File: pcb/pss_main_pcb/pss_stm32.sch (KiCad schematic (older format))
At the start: 24 parts, among them J5 STM32_Prog, SW1 Hot Air Gun Input, SW2 Soldering Iron Input, SW3 SW_Push, U5 STM32F030K6Tx

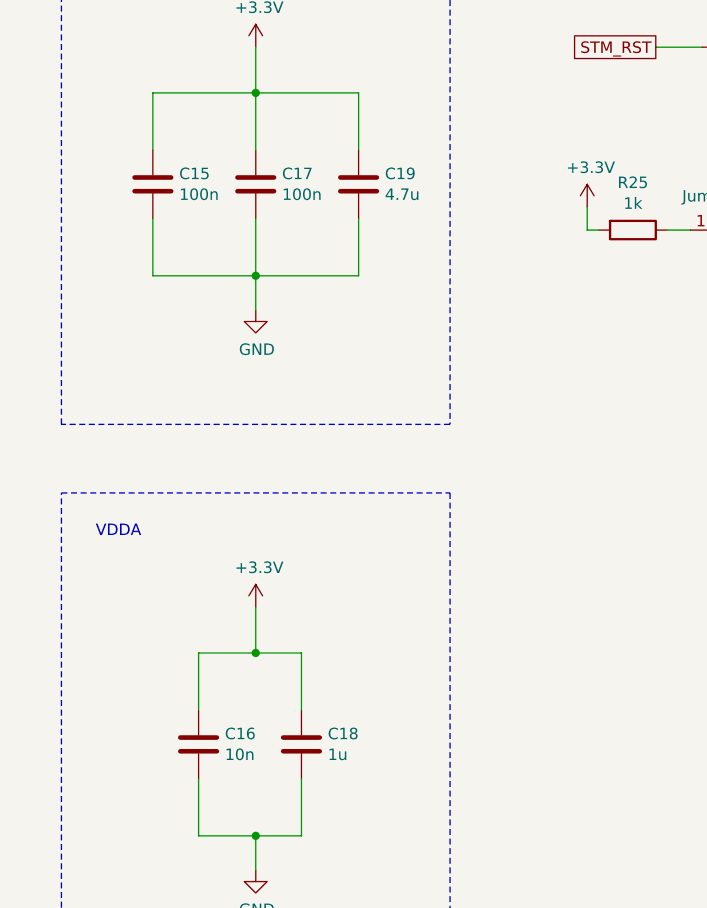
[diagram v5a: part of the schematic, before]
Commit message: Change footprints
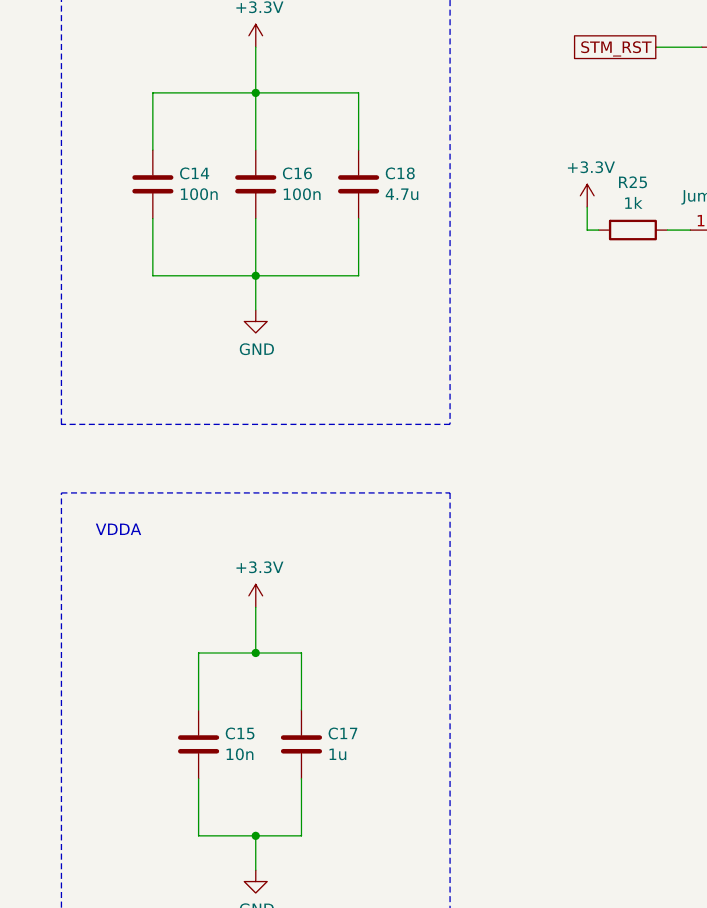
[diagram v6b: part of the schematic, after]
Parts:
- renumbered C15 to C14, C16 to C15, C17 to C16, C18 to C17, C19 to C18
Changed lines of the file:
@@
 $EndComp
 $Comp
-L power:+3.3V #PWR0130
+L power:+3.3V #PWR044
 U 1 1 5EB03E62
 P 5800 2800
-F 0 "#PWR0130" H 5800 2650 50  0001 C CNN
+F 0 "#PWR044" H 5800 2650 50  0001 C CNN
 F 1 "+3.3V" H 5815 2973 50  0000 C CNN
 F 2 "" H 5800 2800 50  0001 C CNN
@@
 	5800 3250 5800 2800
 $Comp
-L power:GND #PWR0131
+L power:GND #PWR043
 U 1 1 5EB04F57
 P 5750 5450
-F 0 "#PWR0131" H 5750 5200 50  0001 C CNN
+F 0 "#PWR043" H 5750 5200 50  0001 C CNN
 F 1 "GND" H 5755 5277 50  0000 C CNN
 F 2 "" H 5750 5450 50  0001 C CNN
@@
 Connection ~ 5750 5350
 $Comp
-L power:+3.3V #PWR0132
+L power:+3.3V #PWR034
 U 1 1 5EB05A07
 P 1550 1100
-F 0 "#PWR0132" H 1550 950 50  0001 C CNN
+F 0 "#PWR034" H 1550 950 50  0001 C CNN
 F 1 "+3.3V" H 1565 1273 50  0000 C CNN
 F 2 "" H 1550 1100 50  0001 C CNN
@@
 	1550 2250 1550 2100
 $Comp
-L Device:C C15
+L Device:C C14
 U 1 1 5EB08B66
 P 1100 1700
-F 0 "C15" H 1215 1746 50  0000 L CNN
+F 0 "C14" H 1215 1746 50  0000 L CNN
 F 1 "100n" H 1215 1655 50  0000 L CNN
 F 2 "Capacitor_SMD:C_1206_3216Metric_Pad1.42x1.75mm_HandSolder" H 1138 1550 50  0001 C CNN
@@
 $EndComp
 $Comp
-L Device:C C19
+L Device:C C18
 U 1 1 5EB07B7B
 P 2000 1700
-F 0 "C19" H 2115 1746 50  0000 L CNN
+F 0 "C18" H 2115 1746 50  0000 L CNN
 F 1 "4.7u" H 2115 1655 50  0000 L CNN
 F 2 "Capacitor_SMD:C_1206_3216Metric_Pad1.42x1.75mm_HandSolder" H 2038 1550 50  0001 C CNN
@@
 $EndComp
 $Comp
-L Device:C C17
+L Device:C C16
 U 1 1 5EB076D7
 P 1550 1700
-F 0 "C17" H 1665 1746 50  0000 L CNN
+F 0 "C16" H 1665 1746 50  0000 L CNN
 F 1 "100n" H 1665 1655 50  0000 L CNN
 F 2 "Capacitor_SMD:C_1206_3216Metric_Pad1.42x1.75mm_HandSolder" H 1588 1550 50  0001 C CNN
@@
 $EndComp
 $Comp
-L power:GND #PWR0133
+L power:GND #PWR035
 U 1 1 5EB05DA1
 P 1550 2250
-F 0 "#PWR0133" H 1550 2000 50  0001 C CNN
+F 0 "#PWR035" H 1550 2000 50  0001 C CNN
 F 1 "GND" H 1555 2077 50  0000 C CNN
 F 2 "" H 1550 2250 50  0001 C CNN
@@
 VDD\n
 $Comp
-L power:+3.3V #PWR0134
+L power:+3.3V #PWR036
 U 1 1 5EB14DAA
 P 1550 3550
-F 0 "#PWR0134" H 1550 3400 50  0001 C CNN
+F 0 "#PWR036" H 1550 3400 50  0001 C CNN
 F 1 "+3.3V" H 1565 3723 50  0000 C CNN
 F 2 "" H 1550 3550 50  0001 C CNN
@@
 	1550 4700 1550 4550
 $Comp
-L Device:C C16
+L Device:C C15
 U 1 1 5EB14DBE
 P 1300 4150
-F 0 "C16" H 1415 4196 50  0000 L CNN
+F 0 "C15" H 1415 4196 50  0000 L CNN
 F 1 "10n" H 1415 4105 50  0000 L CNN
 F 2 "Capacitor_SMD:C_1206_3216Metric_Pad1.42x1.75mm_HandSolder" H 1338 4000 50  0001 C CNN
@@
 $EndComp
 $Comp
-L Device:C C18
+L Device:C C17
 U 1 1 5EB14DC4
 P 1750 4150
-F 0 "C18" H 1865 4196 50  0000 L CNN
+F 0 "C17" H 1865 4196 50  0000 L CNN
 F 1 "1u" H 1865 4105 50  0000 L CNN
 F 2 "Capacitor_SMD:C_1206_3216Metric_Pad1.42x1.75mm_HandSolder" H 1788 4000 50  0001 C CNN
@@
 $EndComp
 $Comp
-L power:GND #PWR0135
+L power:GND #PWR037
 U 1 1 5EB14DD0
 P 1550 4700
-F 0 "#PWR0135" H 1550 4450 50  0001 C CNN
+F 0 "#PWR037" H 1550 4450 50  0001 C CNN
 F 1 "GND" H 1555 4527 50  0000 C CNN
 F 2 "" H 1550 4700 50  0001 C CNN
@@
 AR Path="/5EB3C4EE" Ref="#PWR?"  Part="1"
 AR Path="/5EE027BC/5EB3C4EE" Ref="#PWR?"  Part="1"
-AR Path="/5EE5A305/5EB3C4EE" Ref="#PWR0136"  Part="1"
-F 0 "#PWR0136" H 600 6000 50  0001 C CNN
+AR Path="/5EE5A305/5EB3C4EE" Ref="#PWR032"  Part="1"
+F 0 "#PWR032" H 600 6000 50  0001 C CNN
 F 1 "GND" H 605 6077 50  0000 C CNN
 F 2 "" H 600 6250 50  0001 C CNN
@@
 AR Path="/5EB3C512" Ref="#PWR?"  Part="1"
 AR Path="/5EE027BC/5EB3C512" Ref="#PWR?"  Part="1"
-AR Path="/5EE5A305/5EB3C512" Ref="#PWR0137"  Part="1"
-F 0 "#PWR0137" H 3050 6050 50  0001 C CNN
+AR Path="/5EE5A305/5EB3C512" Ref="#PWR039"  Part="1"
+F 0 "#PWR039" H 3050 6050 50  0001 C CNN
 F 1 "GND" H 3055 6127 50  0000 C CNN
 F 2 "" H 3050 6300 50  0001 C CNN
@@
 $EndComp
 $Comp
-L power:GND #PWR0138
+L power:GND #PWR042
 U 1 1 5EB64547
 P 4850 1200
-F 0 "#PWR0138" H 4850 950 50  0001 C CNN
+F 0 "#PWR042" H 4850 950 50  0001 C CNN
 F 1 "GND" H 4855 1027 50  0000 C CNN
 F 2 "" H 4850 1200 50  0001 C CNN
@@
 	3700 2150 3750 2150
 $Comp
-L power:GND #PWR0139
+L power:GND #PWR041
 U 1 1 5EB6B6D2
 P 4350 2000
-F 0 "#PWR0139" H 4350 1750 50  0001 C CNN
+F 0 "#PWR041" H 4350 1750 50  0001 C CNN
 F 1 "GND" H 4355 1827 50  0000 C CNN
 F 2 "" H 4350 2000 50  0001 C CNN
@@
 	4000 1900 3950 1900
 $Comp
-L power:+3.3V #PWR0140
+L power:+3.3V #PWR038
 U 1 1 5EB6E1EF
 P 3000 1800
-F 0 "#PWR0140" H 3000 1650 50  0001 C CNN
+F 0 "#PWR038" H 3000 1650 50  0001 C CNN
 F 1 "+3.3V" H 3015 1973 50  0000 C CNN
 F 2 "" H 3000 1800 50  0001 C CNN
@@
 AR Path="/5EC370A7" Ref="#PWR?"  Part="1"
 AR Path="/5EE027BC/5EC370A7" Ref="#PWR?"  Part="1"
-AR Path="/5EE5A305/5EC370A7" Ref="#PWR0141"  Part="1"
-F 0 "#PWR0141" H 600 7150 50  0001 C CNN
+AR Path="/5EE5A305/5EC370A7" Ref="#PWR033"  Part="1"
+F 0 "#PWR033" H 600 7150 50  0001 C CNN
 F 1 "GND" H 605 7227 50  0000 C CNN
 F 2 "" H 600 7400 50  0001 C CNN
@@
 AR Path="/5EC370AF" Ref="#PWR?"  Part="1"
 AR Path="/5EE027BC/5EC370AF" Ref="#PWR?"  Part="1"
-AR Path="/5EE5A305/5EC370AF" Ref="#PWR0142"  Part="1"
-F 0 "#PWR0142" H 3050 7250 50  0001 C CNN
+AR Path="/5EE5A305/5EC370AF" Ref="#PWR040"  Part="1"
+F 0 "#PWR040" H 3050 7250 50  0001 C CNN
 F 1 "GND" H 3055 7327 50  0000 C CNN
 F 2 "" H 3050 7500 50  0001 C CNN
@@
 	10400 1150 10050 1150
 $Comp
-L power:+3.3V #PWR0143
+L power:+3.3V #PWR045
 U 1 1 5ED1D948
 P 8600 1000
-F 0 "#PWR0143" H 8600 850 50  0001 C CNN
+F 0 "#PWR045" H 8600 850 50  0001 C CNN
 F 1 "+3.3V" H 8615 1173 50  0000 C CNN
 F 2 "" H 8600 1000 50  0001 C CNN
@@
 	8600 1150 9000 1150
 $Comp
-L power:GND #PWR0144
+L power:GND #PWR047
 U 1 1 5ED24BD5
 P 10650 1850
-F 0 "#PWR0144" H 10650 1600 50  0001 C CNN
+F 0 "#PWR047" H 10650 1600 50  0001 C CNN
 F 1 "GND" H 10655 1677 50  0000 C CNN
 F 2 "" H 10650 1850 50  0001 C CNN
@@
 	9300 1800 9750 1800
 $Comp
-L power:GND #PWR0145
+L power:GND #PWR048
 U 1 1 5ED2F5CE
 P 10650 2650
-F 0 "#PWR0145" H 10650 2400 50  0001 C CNN
+F 0 "#PWR048" H 10650 2400 50  0001 C CNN
 F 1 "GND" H 10655 2477 50  0000 C CNN
 F 2 "" H 10650 2650 50  0001 C CNN
@@
 	9600 4150 9600 3950
 $Comp
-L power:GND #PWR0146
+L power:GND #PWR046
 U 1 1 5EC6DA9A
 P 9400 4600
-F 0 "#PWR0146" H 9400 4350 50  0001 C CNN
+F 0 "#PWR046" H 9400 4350 50  0001 C CNN
 F 1 "GND" H 9405 4427 50  0000 C CNN
 F 2 "" H 9400 4600 50  0001 C CNN

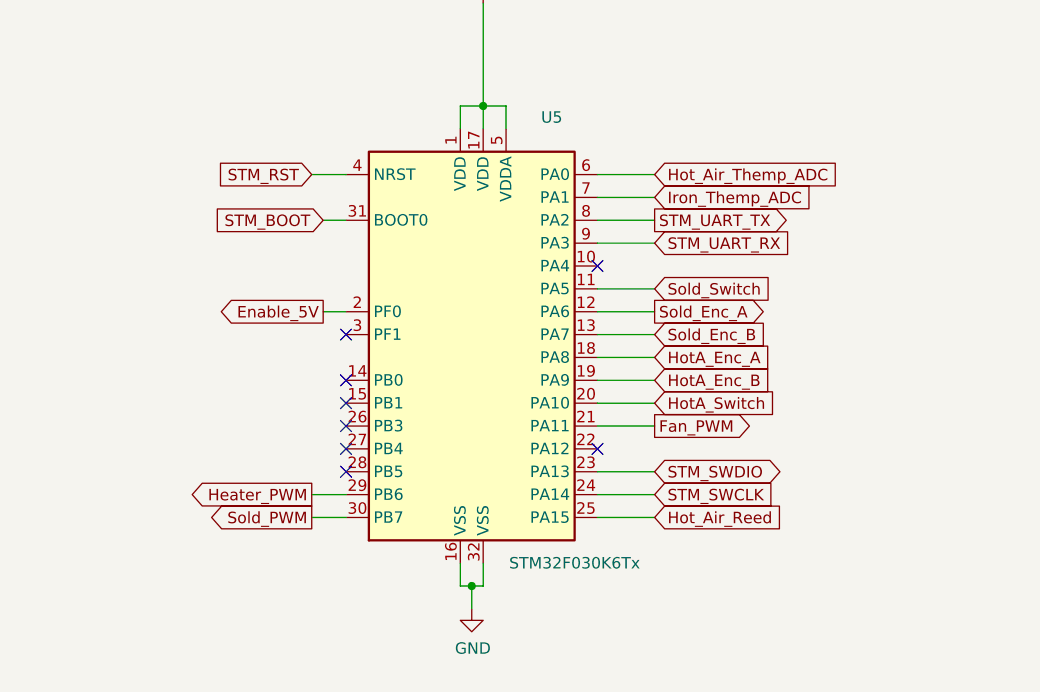
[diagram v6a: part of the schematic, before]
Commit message: Add new routes
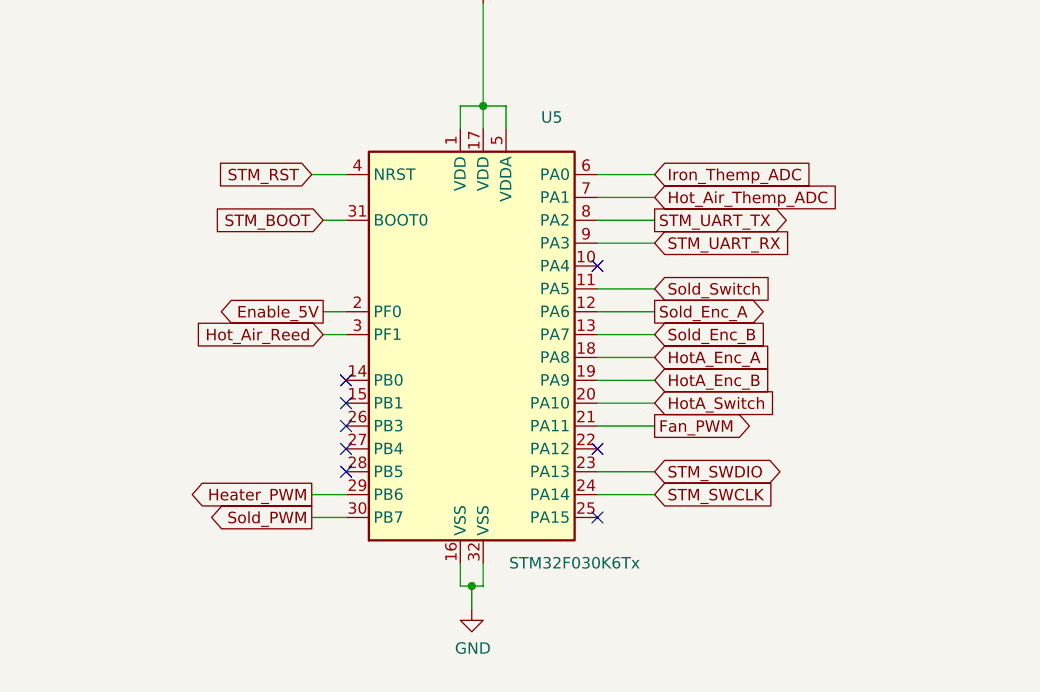
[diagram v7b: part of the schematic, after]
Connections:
- net Hot_Air_Reed: now also U5.3 (PF1); no longer U5.25 (PA15)
- net Hot_Air_Themp_ADC: now also U5.7 (PA1); no longer U5.6 (PA0)
- net Iron_Themp_ADC: now also U5.6 (PA0); no longer U5.7 (PA1)
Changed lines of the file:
@@
 Wire Wire Line
 	5100 3750 5200 3750
-NoConn ~ 5200 4250
 $Comp
 L Device:Rotary_Encoder_Switch SW?
@@
 Wire Wire Line
 	3050 7400 3050 7500
+Text GLabel 6550 3550 2    50   Input ~ 0
+Iron_Themp_ADC
 Text GLabel 6550 3650 2    50   Input ~ 0
-Iron_Themp_ADC
-Text GLabel 6550 3550 2    50   Input ~ 0
 Hot_Air_Themp_ADC
 Wire Wire Line
@@
 Wire Wire Line
 	6550 4950 6300 4950
-Text GLabel 6550 5050 2    50   Input ~ 0
+Text GLabel 5100 4250 0    50   Input ~ 0
 Hot_Air_Reed
-Wire Wire Line
-	6550 5050 6300 5050
 Text GLabel 5050 5050 0    50   Output ~ 0
 Sold_PWM
@@
 Wire Wire Line
 	8600 2600 9000 2600
+Wire Wire Line
+	5200 4250 5100 4250
+NoConn ~ 6300 5050
 $EndSCHEMATC

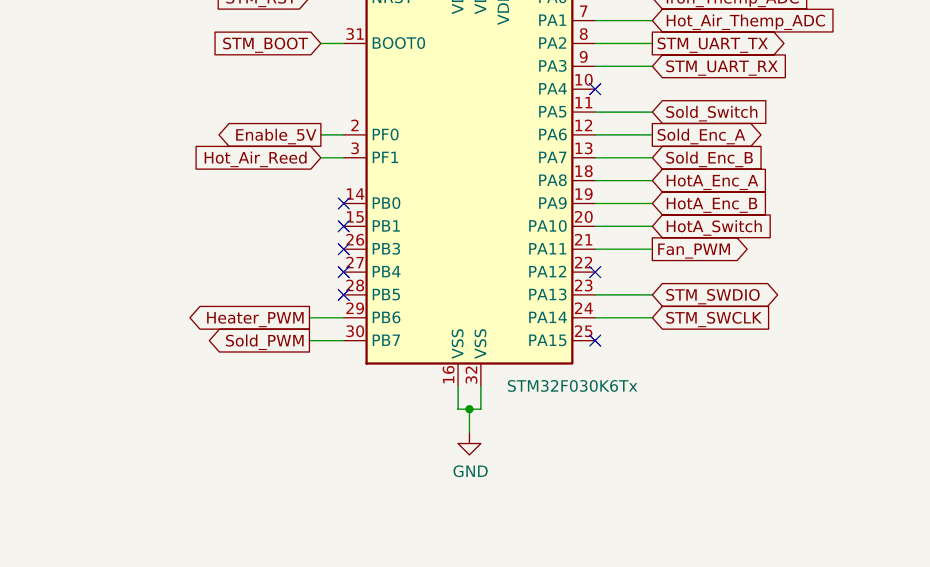
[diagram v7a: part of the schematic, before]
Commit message: Add routes for low power rails
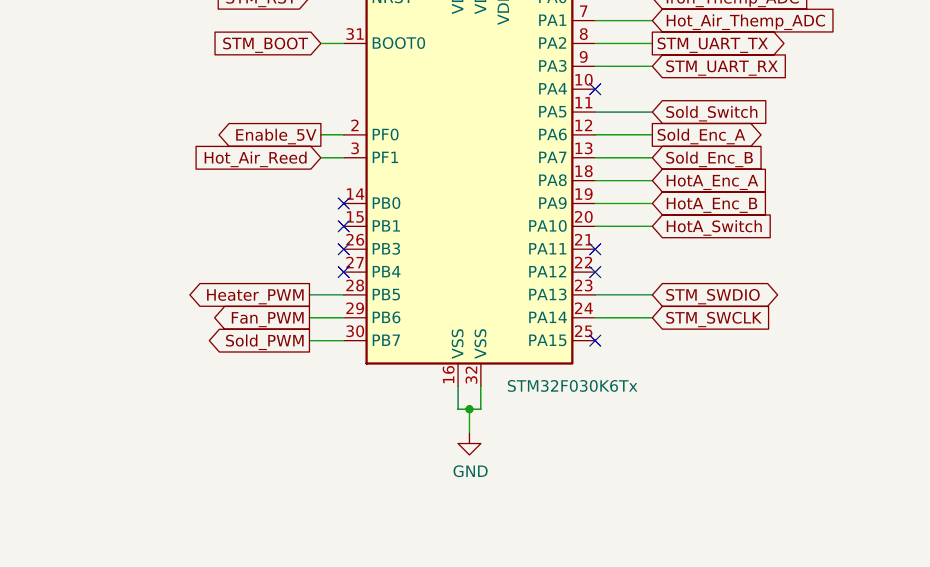
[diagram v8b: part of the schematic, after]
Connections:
- net Fan_PWM: now also U5.29 (PB6); no longer U5.21 (PA11)
- net Heater_PWM: now also U5.28 (PB5); no longer U5.29 (PB6)
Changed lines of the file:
@@
 Wire Wire Line
 	6300 4550 6550 4550
-Text GLabel 6550 4650 2    50   Output ~ 0
+Text GLabel 5050 4950 0    50   Output ~ 0
 Fan_PWM
-Wire Wire Line
-	6550 4650 6300 4650
 Text GLabel 6550 4950 2    50   Input ~ 0
 STM_SWCLK
@@
 Wire Wire Line
 	5200 5050 5050 5050
-Text GLabel 5050 4950 0    50   Output ~ 0
+Text GLabel 5050 4850 0    50   Output ~ 0
 Heater_PWM
-Wire Wire Line
-	5200 4950 5050 4950
 Text GLabel 5100 4150 0    50   Output ~ 0
 Enable_5V
@@
 NoConn ~ 5200 4650
 NoConn ~ 5200 4750
-NoConn ~ 5200 4850
 NoConn ~ 6300 4750
 $Comp
@@
 	5200 4250 5100 4250
 NoConn ~ 6300 5050
+Wire Wire Line
+	5050 4850 5200 4850
+Wire Wire Line
+	5200 4950 5050 4950
+NoConn ~ 6300 4650
 $EndSCHEMATC
